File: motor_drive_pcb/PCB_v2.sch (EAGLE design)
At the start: 25 parts, among them IC2 MCP604P, Q1 MOSFET-NCH-FQP30N06L, Q2 MOSFET-NCH-FQP30N06L

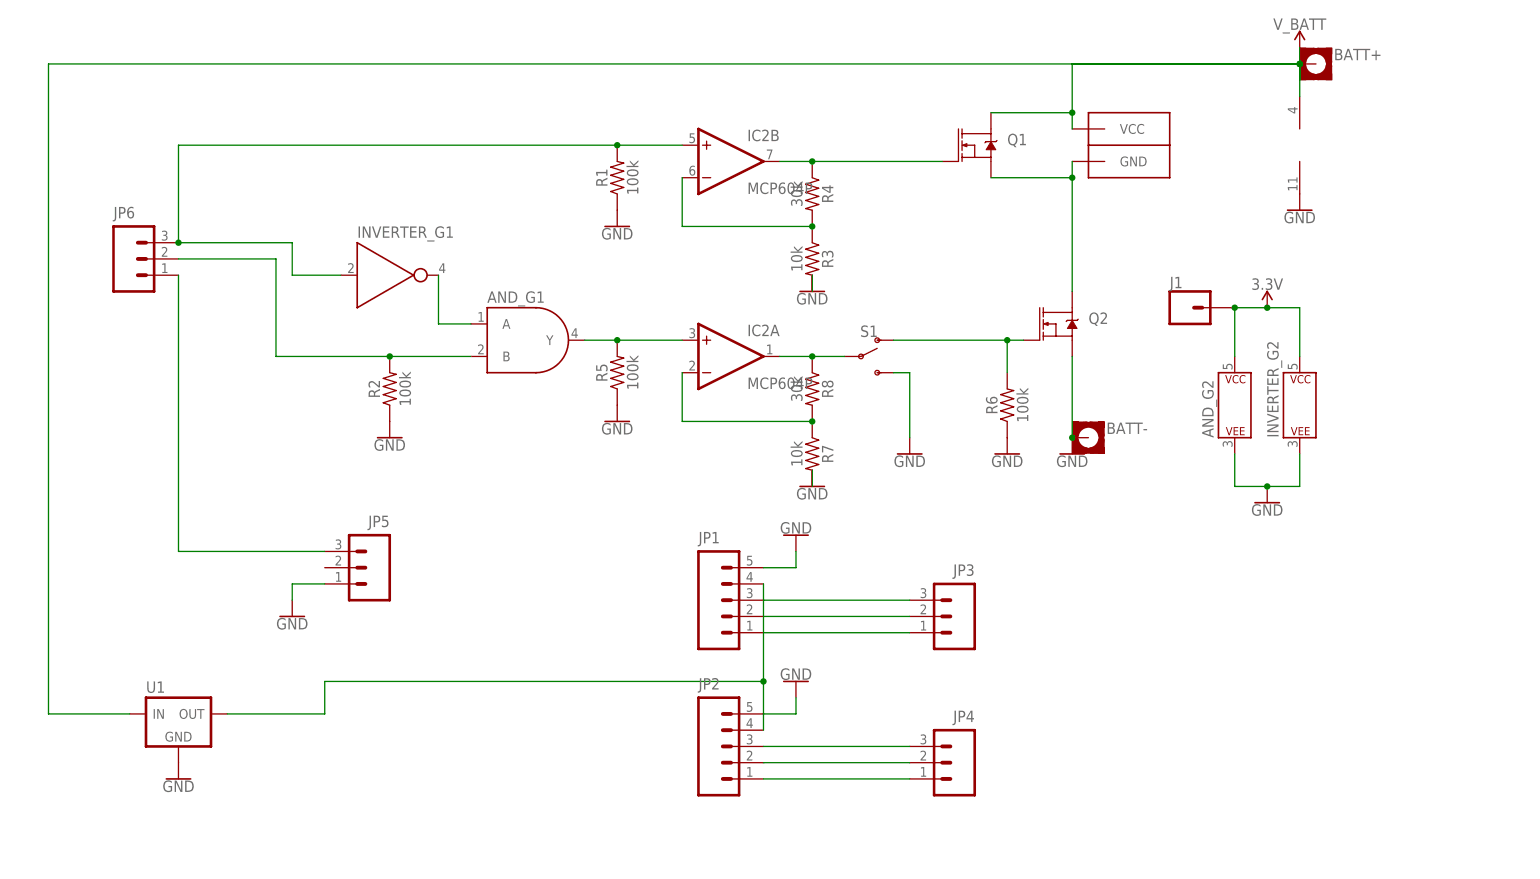
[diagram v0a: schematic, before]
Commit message: updated pcb and encoder schematics and boards
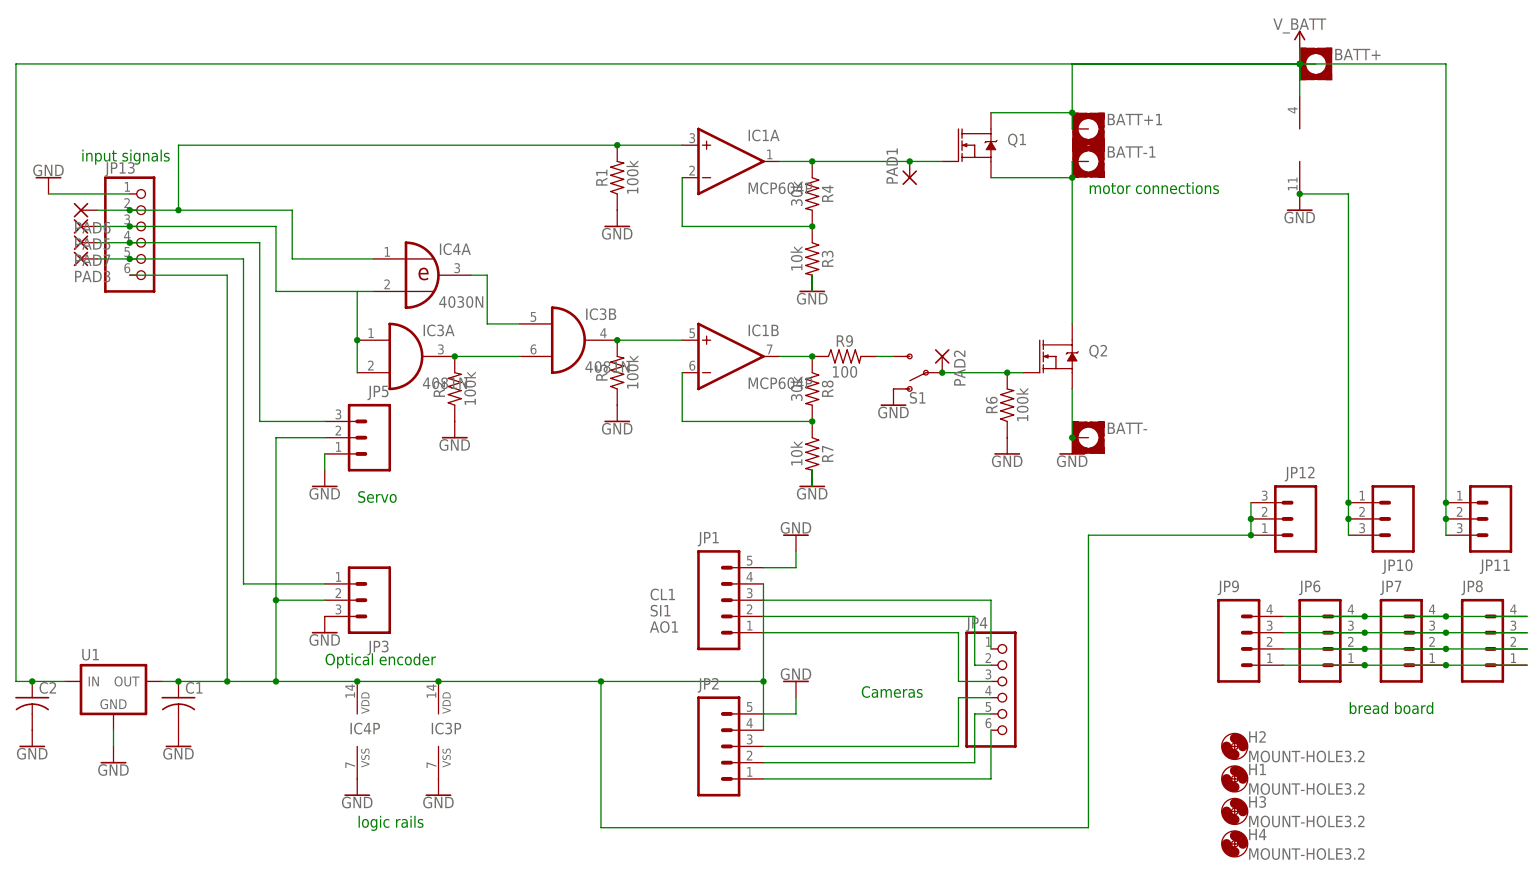
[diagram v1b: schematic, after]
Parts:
- removed AND_: (no value), SparkFun-IC-Logic:74LVC08SE
- removed CONN1: ANDERSON_PP_DOUBLEVERTICAL, ee192:ANDERSON_PP_DOUBLEVERTICAL
- removed IC2: MCP604P, linear:MCP604P
- removed INVERTER_: (no value), SparkFun-IC-Logic:74HC1G04
- removed J1: (no value), SparkFun-Connectors:CONN_01
- added BATT+1, BATT-1: MOUNT-PAD-SQUARE3.0, holes:MOUNT-PAD-SQUARE3.0
- added C1, C2: (no value), bt_rcl:C-075PTH
- added H1, H2, H3, H4: MOUNT-HOLE3.2, holes:MOUNT-HOLE3.2
- added IC1: MCP604P, linear:MCP604P
- added IC3: 4081N, 40xx:4081N
- added IC4: 4030N, 40xx:4030N
- added JP10, JP11, JP12: (no value), ee192:M03PTH
- added JP13: (no value), pinhead:PINHD-1X6
- added JP7, JP8, JP9: (no value), ee192:M04PTH
- added PAD1, PAD2, PAD3, PAD5, PAD6, PAD7: (no value), wirepad:2,15/1,0
- added R9: 100, SparkFun-Resistors:10KOHM-HORIZ-1/4W-1%
- JP4: device ee192:M03PTH -> pinhead:PINHD-1X6
- JP6: device ee192:M03PTH -> ee192:M04PTH
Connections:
- removed net 3.3V: AND_G2.P$V+, INVERTER_G2.P$V+, J1.1
- removed net N$12: JP1.1, JP3.1
- removed net N$13: JP1.2, JP3.2
- removed net N$14: JP1.3, JP3.3
- removed net N$17: AND_G1.B, JP6.2, R2.2
- new net AO1: JP1.1, JP4.3
- new net CL1: JP1.3, JP4.1
- new net N$19: JP13.5, JP3.1, PAD3.P
- new net N$20: IC1B.+IN, IC3B.O, R5.2
- new net N$21: IC3A.O, IC3B.I1, R2.2
- new net N$22: JP6.4, JP7.4, JP8.4, JP9.4
- new net N$23: JP6.3, JP7.3, JP8.3, JP9.3
- new net N$24: JP6.2, JP7.2, JP8.2, JP9.2
- new net N$25: JP6.1, JP7.1, JP8.1, JP9.1
- new net N$26: IC3A.I0, IC3A.I1, IC4A.I1, JP13.3, PAD5.P
- new net SI1: JP1.2, JP4.2
- net GND: now also C1.-, C2.-, IC1P.V-, IC3P.VSS, IC4P.VSS, JP10.1, JP10.2, JP10.3, JP13.1, JP3.3, S1.O; no longer AND_G2.P$V-, IC2P.V-, INVERTER_G2.P$V-, S1.S
- net N$1: now also IC1A.-IN; no longer IC2B.-IN
- net N$10: now also JP4.5; no longer JP4.2
- net N$11: now also JP4.4; no longer JP4.3
- net N$15: now also JP13.4, PAD7.P; no longer JP6.1
- net N$16: now also IC1A.+IN, IC4A.I0, JP13.2, PAD6.P; no longer IC2B.+IN, INVERTER_G1.A, JP6.3
- net N$18: now also C1.+, IC3P.VDD, IC4P.VDD, JP12.1, JP12.2, JP12.3, JP13.6, JP3.2, JP5.2
- net N$2: now also IC1A.OUT, PAD1.P; no longer IC2B.OUT
- net N$3: now also IC1B.-IN; no longer IC2A.-IN
- net N$4: now also R9.2, S1.S; no longer AND_G1.Y, IC2A.+IN, R5.2
- net N$5: now also PAD2.P, S1.P; no longer S1.O
- net N$6: now also BATT-1.MOUNT; no longer CONN1.GND
- net N$7: now also IC1B.OUT, R9.1; no longer IC2A.OUT, S1.P
- net N$8: now also IC3B.I0, IC4A.O; no longer AND_G1.A, INVERTER_G1.Y
- net N$9: now also JP4.6; no longer JP4.1
- net V_BATT: now also BATT+1.MOUNT, C2.+, IC1P.V+, JP11.1, JP11.2, JP11.3; no longer CONN1.VCC, IC2P.V+
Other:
- note added: "Cameras"
- note added: "Optical encoder"
- note added: "Servo"
- note added: "bread board"
- note added: "input signals"
- note added: "logic rails"
- note added: "motor connections"
- moved on the sheet: JP3, JP5, Q2, R2, S1, U1
